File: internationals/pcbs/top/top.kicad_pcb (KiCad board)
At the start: 2 copper layers, 170 x 147 mm, 0 parts

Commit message: pcbs: top: feat: complete pcb
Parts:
- added G*** (x2): LOGO, LOGO, B.Cu at (97.0, 100.0)
- added H1: MountingHole-M3, MountingHole:MountingHole_3.2mm_M3_Pad_Via, F.Cu at (26.0, 85.0)
- added H10: MountingHole-M3, MountingHole:MountingHole_3.2mm_M3_Pad_Via, F.Cu at (55.5, 124.7)
- added H11: MountingHole-M3, MountingHole:MountingHole_3.2mm_M3_Pad_Via, F.Cu at (122.5, 122.5)
- added H12: MountingHole-M3, MountingHole:MountingHole_3.2mm_M3_Pad_Via, F.Cu at (116.0, 158.0)
- added H13: MountingHole-M3, MountingHole:MountingHole_3.2mm_M3_Pad_Via, F.Cu at (26.0, 115.0)
- added H14: MountingHole-M3, MountingHole:MountingHole_3.2mm_M3_Pad_Via, F.Cu at (174.0, 100.0)
- added H15: MountingHole-M3, MountingHole:MountingHole_3.2mm_M3_Pad_Via, F.Cu at (122.5, 65.5)
- added H16: MountingHole-M3, MountingHole:MountingHole_3.2mm_M3_Pad_Via, F.Cu at (144.5, 124.7)
- added H17: MountingHole-M3, MountingHole:MountingHole_3.2mm_M3_Pad_Via, F.Cu at (75.3, 144.5)
- added H18: MountingHole-M3, MountingHole:MountingHole_3.2mm_M3_Pad_Via, F.Cu at (100.0, 178.0)
- added H19: MountingHole-M3, MountingHole:MountingHole_3.2mm_M3_Pad_Via, F.Cu at (27.7, 70.8)
- added H2: MountingHole-M3, MountingHole:MountingHole_3.2mm_M3_Pad_Via, F.Cu at (172.3, 70.8)
- added H20: MountingHole-M3, MountingHole:MountingHole_3.2mm_M3_Pad_Via, F.Cu at (174.0, 115.0)
- added H21: MountingHole-M3, MountingHole:MountingHole_3.2mm_M3_Pad_Via, F.Cu at (77.5, 65.5)
- added H22: MountingHole-M3, MountingHole:MountingHole_3.2mm_M3_Pad_Via, F.Cu at (144.5, 75.3)
- added H23: MountingHole-M3, MountingHole:MountingHole_3.2mm_M3_Pad_Via, F.Cu at (124.7, 144.5)
- added H24: MountingHole-M6, MountingHole:MountingHole_6.4mm_M6_Pad_Via, F.Cu at (76.0, 167.0)
- added H25: MountingHole-M3, MountingHole:MountingHole_3.2mm_M3_Pad_Via, F.Cu at (87.0, 139.0)
- added H26: MountingHole-M3, MountingHole:MountingHole_3.2mm_M3_Pad_Via, F.Cu at (113.0, 139.0)
- added H27: MountingHole-M2.5, MountingHole:MountingHole_2.7mm_M2.5_Pad_Via, F.Cu at (95.2, 137.7)
- added H28: MountingHole-M2.5, MountingHole:MountingHole_2.7mm_M2.5_Pad_Via, F.Cu at (95.2, 158.3)
- added H29: MountingHole-M2.5, MountingHole:MountingHole_2.7mm_M2.5_Pad_Via, F.Cu at (104.8, 137.7)
- added H3: MountingHole-M3, MountingHole:MountingHole_3.2mm_M3_Pad_Via, F.Cu at (124.7, 55.5)
- added H30: MountingHole-M2.5, MountingHole:MountingHole_2.7mm_M2.5_Pad_Via, F.Cu at (104.8, 158.3)
- added H4: MountingHole-M3, MountingHole:MountingHole_3.2mm_M3_Pad_Via, F.Cu at (55.5, 75.3)
- added H5: MountingHole-M3, MountingHole:MountingHole_3.2mm_M3_Pad_Via, F.Cu at (77.5, 122.5)
- added H6: MountingHole-M3, MountingHole:MountingHole_3.2mm_M3_Pad_Via, F.Cu at (87.0, 167.0)
- added H7: MountingHole-M3, MountingHole:MountingHole_3.2mm_M3_Pad_Via, F.Cu at (26.0, 100.0)
- added H8: MountingHole-M3, MountingHole:MountingHole_3.2mm_M3_Pad_Via, F.Cu at (174.0, 85.0)
- added H9: MountingHole-M3, MountingHole:MountingHole_3.2mm_M3_Pad_Via, F.Cu at (75.3, 55.5)
- added J1: Header-01x08, Connector_PinHeader_2.54mm:PinHeader_1x08_P2.54mm_Vertical, F.Cu at (83.1, 75.5)
- added J10: JST-XH-S4B, Connector_JST:JST_XH_S4B-XH-A_1x04_P2.50mm_Horizontal, B.Cu at (103.8, 165.0)
- added J11: JST-XH-B6B, Connector_JST:JST_XH_B6B-XH-A_1x06_P2.50mm_Vertical, B.Cu at (65.5, 93.8)
- added J12: 5V-JST-XH-B2B, Connector_JST:JST_XH_B2B-XH-A_1x02_P2.50mm_Vertical, F.Cu at (152.5, 70.5)
- added J13: Header-01x03, Connector_PinHeader_2.54mm:PinHeader_1x03_P2.54mm_Vertical, F.Cu at (136.5, 98.7)
- added J2: 5V-JST-XH-B2B, Connector_JST:JST_XH_B2B-XH-A_1x02_P2.50mm_Vertical, F.Cu at (162.5, 70.5)
- added J3: Debug-JST-XH-B3B, Connector_JST:JST_XH_B3B-XH-A_1x03_P2.50mm_Vertical, F.Cu at (168.7, 130.0)
- added J4: 5V-JST-XH-B2B, Connector_JST:JST_XH_B2B-XH-A_1x02_P2.50mm_Vertical, F.Cu at (45.0, 70.5)
- added J5: 5V-JST-XH-B2B, Connector_JST:JST_XH_B2B-XH-A_1x02_P2.50mm_Vertical, F.Cu at (89.6, 173.7)
- added J6: IMU-UART-JST-XH-B2B, Connector_JST:JST_XH_B2B-XH-A_1x02_P2.50mm_Vertical, F.Cu at (36.3, 72.2)
- added J7: Header-01x03, Connector_PinHeader_2.54mm:PinHeader_1x03_P2.54mm_Vertical, F.Cu at (83.5, 122.5)
- added J8: I2C0-JST-XH-B2B, Connector_JST:JST_XH_B2B-XH-A_1x02_P2.50mm_Vertical, F.Cu at (137.8, 138.0)
- added J9: I2C1-JST-XH-B2B, Connector_JST:JST_XH_B2B-XH-A_1x02_P2.50mm_Vertical, F.Cu at (147.4, 137.9)
- added M1: MotorDriver1A-XH-B4B, Connector_JST:JST_XH_B4B-XH-A_1x04_P2.50mm_Vertical, B.Cu at (93.2, 40.5)
- added M2: MotorDriver1B-XH-B4B, Connector_JST:JST_XH_B4B-XH-A_1x04_P2.50mm_Vertical, B.Cu at (114.2, 40.5)
- added M3: MotorDriver2A-XH-B4B, Connector_JST:JST_XH_B4B-XH-A_1x04_P2.50mm_Vertical, B.Cu at (93.2, 47.5)
- added M4: MotorDriver2B-XH-B4B, Connector_JST:JST_XH_B4B-XH-A_1x04_P2.50mm_Vertical, B.Cu at (114.2, 47.5)
- added P1: MotorDriver1-Power-XH-B2B, Connector_JST:JST_XH_B2B-XH-A_1x02_P2.50mm_Vertical, B.Cu at (106.2, 129.5)
- added P2: MotorDriver2-Power-XH-B2B, Connector_JST:JST_XH_B2B-XH-A_1x02_P2.50mm_Vertical, B.Cu at (96.2, 129.5)
- added R1: R, PCM_Resistor_THT_AKL:R_Axial_DIN0204_L3.6mm_D1.6mm_P5.08mm_Horizontal, F.Cu at (136.5, 91.0)
- added SW1: SW_Push, Button_Switch_THT:SW_PUSH_6mm, F.Cu at (114.8, 174.6)
- added SW10: MotorDriver-Power-SW-SPDT-XH-B2B, Connector_JST:JST_XH_B2B-XH-A_1x02_P2.50mm_Vertical, B.Cu at (75.0, 156.0)
- added SW2: SW_Push, Button_Switch_THT:SW_PUSH_6mm, F.Cu at (124.8, 174.6)
- added U1: Raspberry-Pi-Pico, PorridgePi-Personal:Raspberry-Pi-Pico, F.Cu at (111.1, 75.9)
- added U2: OpenMV-H7, PorridgePi-Personal:OpenMV-H7, F.Cu at (83.1, 100.0)
- added U3: MINI560 5V, PorridgePi-Personal:MINI560, F.Cu at (76.3, 134.0)
- added kibuzzard-666B0E6A: G***, kibuzzard-666B0E6A, F.Cu at (100.0, 60.5)
- added kibuzzard-666D6A28: G***, kibuzzard-666D6A28, F.Cu at (92.9, 174.9)
- added kibuzzard-666D6A28: G***, kibuzzard-666D6A28, F.Cu at (163.8, 74.9)
- added kibuzzard-666D6A28: G***, kibuzzard-666D6A28, F.Cu at (46.2, 74.9)
- added kibuzzard-666D6A28: G***, kibuzzard-666D6A28, F.Cu at (153.8, 74.9)
- added kibuzzard-666D6A28: G***, kibuzzard-666D6A28, B.Cu at (46.3, 72.9)
- added kibuzzard-666D6A28: G***, kibuzzard-666D6A28, B.Cu at (163.7, 72.9)
- added kibuzzard-666D6A28: G***, kibuzzard-666D6A28, B.Cu at (153.7, 72.9)
- added kibuzzard-666D6AFC: G***, kibuzzard-666D6AFC, F.Cu at (100.0, 168.2)
- added kibuzzard-666D6AFC: G***, kibuzzard-666D6AFC, B.Cu at (52.2, 137.8)
- added kibuzzard-666D6AFC: G***, kibuzzard-666D6AFC, B.Cu at (108.0, 169.2)
- added kibuzzard-666D6B3A: G***, kibuzzard-666D6B3A, F.Cu at (47.4, 138.0)
- added kibuzzard-666D6C08: G***, kibuzzard-666D6C08, F.Cu at (139.0, 142.4)
- added kibuzzard-666D6C08: G***, kibuzzard-666D6C08, B.Cu at (139.0, 140.5)
- added kibuzzard-666D6C3F: G***, kibuzzard-666D6C3F, F.Cu at (148.7, 142.3)
- added kibuzzard-666D6C3F: G***, kibuzzard-666D6C3F, B.Cu at (148.7, 140.6)
- added kibuzzard-666D6C77: G***, kibuzzard-666D6C77, F.Cu at (174.8, 132.0)
- added kibuzzard-666D6C83: G***, kibuzzard-666D6C83, F.Cu at (176.4, 127.4)
- added kibuzzard-666D6C87: G***, kibuzzard-666D6C87, F.Cu at (174.8, 129.4)
- added kibuzzard-666D6D8F: G***, kibuzzard-666D6D8F, F.Cu at (36.8, 75.8)
- added kibuzzard-666D6D8F: G***, kibuzzard-666D6D8F, B.Cu at (36.2, 74.8)
- added kibuzzard-666D6EB8: G***, kibuzzard-666D6EB8, B.Cu at (100.0, 44.0)
- added kibuzzard-666D6EEA: G***, kibuzzard-666D6EEA, F.Cu at (100.0, 45.0)
- added kibuzzard-666D6FA1: G***, kibuzzard-666D6FA1, F.Cu at (171.5, 135.0)
- added kibuzzard-666D6FA1: G***, kibuzzard-666D6FA1, B.Cu at (173.7, 128.9)
- added kibuzzard-666D7734: G***, kibuzzard-666D7734, F.Cu at (68.0, 100.0)
- added kibuzzard-666D7734: G***, kibuzzard-666D7734, B.Cu at (70.0, 100.0)
- added kibuzzard-666D7803: G***, kibuzzard-666D7803, B.Cu at (122.5, 171.2)
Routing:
- net Top-TX1-IMU-RX: track 0.00 -> 142.9 mm
- net Top-RX1-IMU-TX: track 0.00 -> 137.6 mm
- net Button2: track 0.00 -> 106.2 mm, vias 0 -> 1
- net PWM4B: track 0.00 -> 96.1 mm, vias 0 -> 1
- net PWM2B: track 0.00 -> 92.3 mm, vias 0 -> 1
- net PWM4A: track 0.00 -> 89.1 mm, vias 0 -> 1
- net Top-TX0-Cam-RX3: track 0.00 -> 87.0 mm
- net PWM2A: track 0.00 -> 86.8 mm, vias 0 -> 1
- net Top-RX0-Cam-TX3: track 0.00 -> 85.3 mm
- net GND: track 0.00 -> 82.5 mm, vias 0 -> 16
- net Button1: track 0.00 -> 81.2 mm, vias 0 -> 1
- net PWM3B: track 0.00 -> 79.1 mm
- net PWM1B: track 0.00 -> 78.4 mm, vias 0 -> 1
- net PWM3A: track 0.00 -> 74.0 mm, vias 0 -> 1
- net PWM1A: track 0.00 -> 71.6 mm, vias 0 -> 1
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- added copper zone on B.Cu, net +12V
- added copper zone on F.Cu, net +5V
- added copper zone on B.Cu, net GND
- added copper zone on F.Cu, net GND
- added copper zone on B.Cu, net GND1
- added copper zone on F.Cu, net GND1
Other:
- board text added: "A"
- board text added: "B"
- board text added: "DRV PWR"
- board text added: "M1"
- board text added: "M2"
- board text added: "M3"
- board text added: "M4"
- board text added: "P9 P8 P7 P6 P3 P2 P1 P0"
- board text added: "Team Gloves Zhou Yikun & Zachary Ang Club Automatica Singapore 2024"

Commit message: pcbs: top: feat: add JLCJLCJLCJLC silkscreen
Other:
- board text added: "JLCJLCJLCJLC"
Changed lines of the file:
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@@
 		(tags "connector JST XH vertical")
 		(property "Reference" "J2"
-			(at 1.25 -3.55 360)
+			(at 1.25 -3.55 0)
 			(layer "F.SilkS")
 			(effects
@@
 		)
 		(property "Value" "5V-JST-XH-B2B"
-			(at 1.25 4.6 360)
+			(at 1.25 4.6 0)
 			(layer "F.Fab")
 			(effects
@@
 		)
 		(fp_text user "${REFERENCE}"
-			(at 1.25 2.7 360)
+			(at 1.25 2.7 0)
 			(layer "F.Fab")
 			(effects
@@
 				(font
 					(size 0.001 0.001)
+					(thickness 0.15)
 				)
 			)
@@
 				(font
 					(size 0.001 0.001)
+					(thickness 0.15)
 				)
 			)
@@
 				(font
 					(size 0.001 0.001)
+					(thickness 0.15)
 				)
 			)
@@
 				(font
 					(size 0.001 0.001)
+					(thickness 0.15)
 				)
 			)
@@
 		)
 		(fp_text user "${REFERENCE}"
-			(at 0 2.54 360)
+			(at 0 2.54 0)
 			(layer "F.Fab")
 			(effects
@@
 				(font
 					(size 0.001 0.001)
+					(thickness 0.15)
 				)
 			)
@@
 				(font
 					(size 0.001 0.001)
+					(thickness 0.15)
 				)
 			)
@@
 		(fp_arc
 			(start 19.42 49.32)
-			(mid 19.213496 49.58881)
+			(mid 19.213497 49.588778)
 			(end 18.89 49.69)
 			(stroke
@@
 		(fp_arc
 			(start 18.89 -1.43)
-			(mid 19.213484 -1.328785)
+			(mid 19.213502 -1.328793)
 			(end 19.42 -1.06)
 			(stroke
@@
 		(fp_arc
 			(start 19.42 49.32)
-			(mid 19.213496 49.58881)
+			(mid 19.213497 49.588778)
 			(end 18.89 49.69)
 			(stroke
@@
 				(font
 					(size 0.001 0.001)
+					(thickness 0.15)
 				)
 			)
@@
 				(font
 					(size 0.001 0.001)
+					(thickness 0.15)
 				)
 			)
@@
 				(font
 					(size 0.001 0.001)
+					(thickness 0.15)
 				)
 			)
@@
 				(font
 					(size 0.001 0.001)
+					(thickness 0.15)
 				)
 			)
@@
 				(font
 					(size 0.001 0.001)
+					(thickness 0.15)
 				)
 			)
@@
 				(font
 					(size 0.001 0.001)
+					(thickness 0.15)
 				)
 			)
@@
 				(xy -1.989139 -0.495902) (xy -1.895559 -0.452869) (xy -1.861408 -0.426913) (xy -1.819057 -0.359973)
 				(xy -1.851843 -0.284836) (xy -1.898974 -0.233607) (xy -1.947473 -0.21653) (xy -2.018511 -0.243852)
-				(xy -2.034221 -0.257515) (xy -2.055396 -0.275273) (xy -2.128484 -0.293033) (xy -2.202254 -0.271858)
+				(xy -2.034221 -0.257516) (xy -2.055396 -0.275273) (xy -2.128484 -0.293033) (xy -2.202254 -0.271858)
 				(xy -2.231626 -0.213115) (xy -2.19679 -0.152322) (xy -2.110041 -0.120902) (xy -2.055738 -0.110485)
 				(xy -1.996652 -0.095628) (xy -1.937568 -0.076673) (xy -1.883265 -0.053962) (xy -1.835622 -0.020321)
@@
 		(tags "connector JST XH vertical")
 		(property "Reference" "J12"
-			(at 1.25 -3.55 360)
+			(at 1.25 -3.55 0)
 			(layer "F.SilkS")
 			(effects
@@
 		)
 		(property "Value" "5V-JST-XH-B2B"
-			(at 1.25 4.6 360)
+			(at 1.25 4.6 0)
 			(layer "F.Fab")
 			(effects
@@
 		)
 		(fp_text user "${REFERENCE}"
-			(at 1.25 2.7 360)
+			(at 1.25 2.7 0)
 			(layer "F.Fab")
 			(effects
@@
 				(font
 					(size 0.001 0.001)
+					(thickness 0.15)
 				)
 			)
@@
 				(font
 					(size 0.001 0.001)
+					(thickness 0.15)
 				)
 			)
@@
 				(font
 					(size 0.001 0.001)
+					(thickness 0.15)
 				)
 			)
@@
 				(font
 					(size 0.001 0.001)
+					(thickness 0.15)
 				)
 			)
@@
 				(xy -2.163593 -0.273907) (xy -2.23668 -0.291667) (xy -2.310451 -0.270492) (xy -2.339822 -0.211749)
 				(xy -2.304986 -0.150956) (xy -2.218238 -0.119536) (xy -2.163934 -0.109119) (xy -2.10485 -0.094261)
-				(xy -2.045765 -0.075307) (xy -1.991462 -0.052596) (xy -1.943818 -0.018955) (xy -1.904714 0.032787)
+				(xy -2.045765 -0.075307) (xy -1.991462 -0.052596) (xy -1.943818 -0.018955) (xy -1.904715 0.032787)
 				(xy -1.878586 0.100581) (xy -1.869877 0.182377) (xy -1.878757 0.265881) (xy -1.905396 0.338798)
 				(xy -1.94638 0.398736) (xy -1.998292 0.443306) (xy -2.073733 0.483531) (xy -2.152512 0.507665) (xy -2.234631 0.51571)
@@
 				(font
 					(size 0.001 0.001)
+					(thickness 0.15)
 				)
 			)
@@
 				(font
 					(size 0.001 0.001)
+					(thickness 0.15)
 				)
 			)
@@
 		(tags "Through hole pin header THT 1x03 2.54mm single row")
 		(property "Reference" "J13"
-			(at 0 -2.33 360)
+			(at 0 -2.33 0)
 			(layer "F.SilkS")
 			(effects
@@
 		)
 		(property "Value" "Header-01x03"
-			(at 0 7.41 360)
+			(at 0 7.41 0)
 			(layer "F.Fab")
 			(effects
@@
 				(font
 					(size 0.001 0.001)
+					(thickness 0.15)
 				)
 			)
@@
 				(font
 					(size 0.001 0.001)
+					(thickness 0.15)
 				)
 			)
@@
 				(font
 					(size 0.001 0.001)
+					(thickness 0.15)
 				)
 			)
@@
 				(font
 					(size 0.001 0.001)
+					(thickness 0.15)
 				)
 			)
@@
 		(tags "connector JST XH vertical")
 		(property "Reference" "J4"
-			(at 1.25 -3.55 360)
+			(at 1.25 -3.55 0)
 			(layer "F.SilkS")
 			(hide yes)
@@
 		)
 		(property "Value" "5V-JST-XH-B2B"
-			(at 1.25 4.6 360)
+			(at 1.25 4.6 0)
 			(layer "F.Fab")
 			(effects
@@
 		)
 		(fp_text user "${REFERENCE}"
-			(at 1.25 2.7 360)
+			(at 1.25 2.7 0)
 			(layer "F.Fab")
 			(effects
@@
 				(font
 					(size 0.001 0.001)
+					(thickness 0.15)
 				)
 			)
@@
 				(font
 					(size 0.001 0.001)
+					(thickness 0.15)
 				)
 			)
@@
 				(font
 					(size 0.001 0.001)
+					(thickness 0.15)
 				)
 				(justify mirror)
@@
 				(font
 					(size 0.001 0.001)
+					(thickness 0.15)
 				)
 				(justify mirror)
@@
 		(tags "connector JST XH vertical")
 		(property "Reference" "SW10"
-			(at 1.25 3.55 360)
+			(at 1.25 3.55 0)
 			(layer "B.SilkS")
 			(effects
@@
 		)
 		(property "Value" "MotorDriver-Power-SW-SPDT-XH-B2B"
-			(at 1.25 -4.6 360)
+			(at 1.25 -4.6 0)
 			(layer "B.Fab")
 			(effects
@@
 		)
 		(fp_text user "${REFERENCE}"
-			(at 1.25 -2.7 360)
+			(at 1.25 -2.7 0)
 			(layer "B.Fab")
 			(effects
@@
 				(font
 					(size 0.001 0.001)
+					(thickness 0.15)
 				)
 				(justify mirror)
@@
 				(font
 					(size 0.001 0.001)
+					(thickness 0.15)
 				)
 				(justify mirror)
@@
 				(font
 					(size 0.001 0.001)
+					(thickness 0.15)
 				)
 				(justify mirror)
@@
 				(font
 					(size 0.001 0.001)
+					(thickness 0.15)
 				)
 				(justify mirror)
@@
 				(font
 					(size 0.001 0.001)
+					(thickness 0.15)
 				)
 				(justify mirror)
@@
 				(font
 					(size 0.001 0.001)
+					(thickness 0.15)
 				)
 				(justify mirror)
@@
 			)
 			(justify mirror)
+		)
+	)
+	(gr_text "JLCJLCJLCJLC"
+		(at 100 183 -0)
+		(layer "B.SilkS")
+		(effects
+			(font
+				(size 0.8 0.8)
+				(thickness 0.15)
+				(bold yes)
+			)
+			(justify mirror)

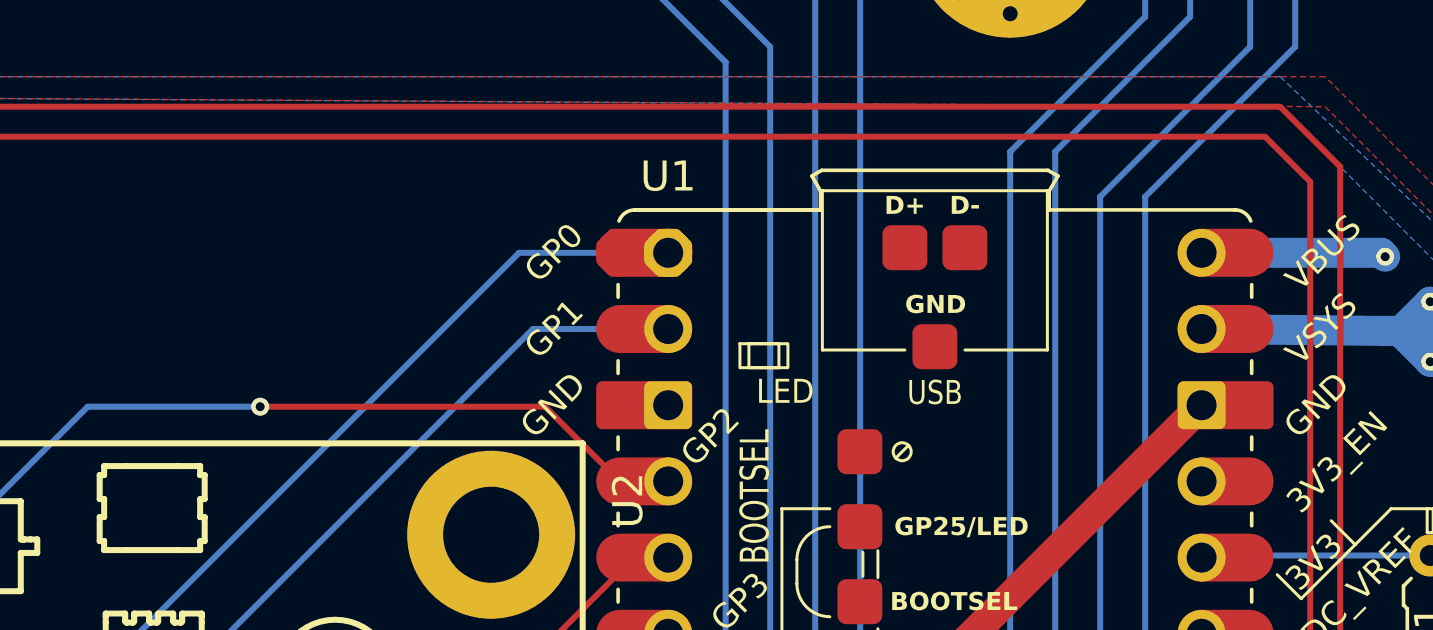
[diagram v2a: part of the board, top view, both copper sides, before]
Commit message: pcbs: feat: add OSHW and Rust Ferris logos
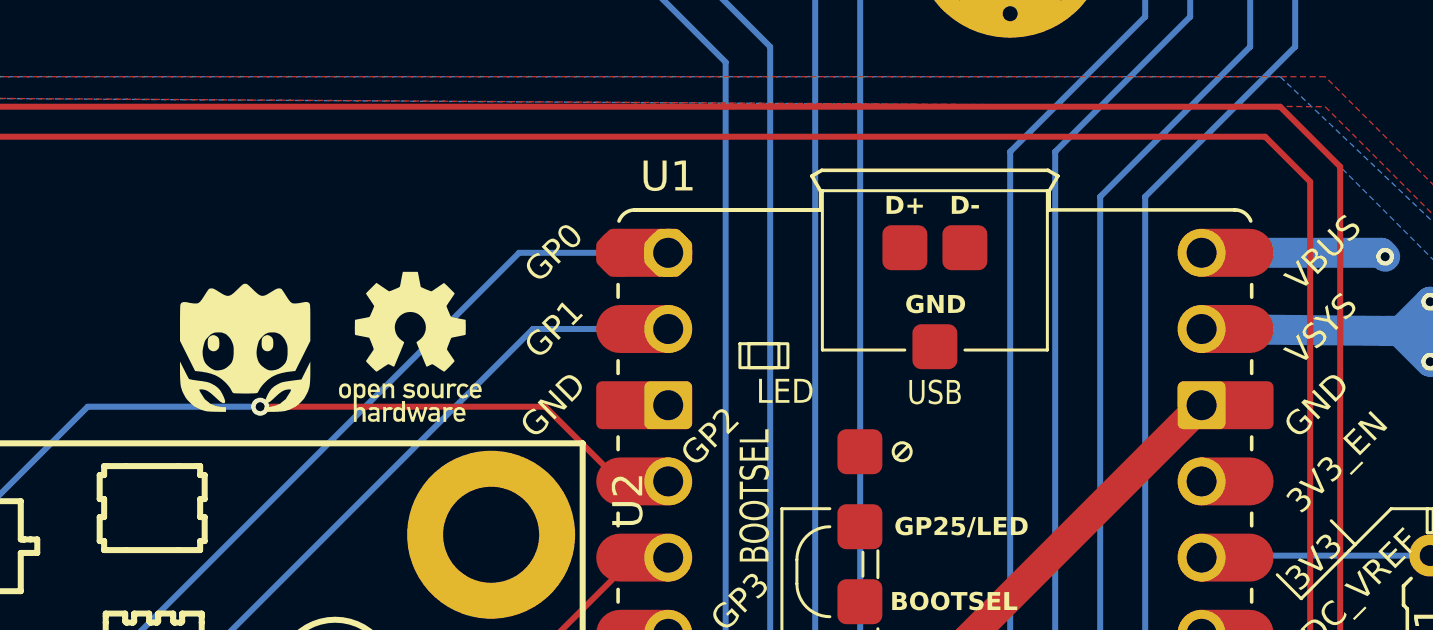
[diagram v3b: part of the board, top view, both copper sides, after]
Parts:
- added G***: LOGO, LOGO, F.Cu at (97.0, 79.0)
- added G***: LOGO, LOGO, F.Cu at (102.5, 79.0)
